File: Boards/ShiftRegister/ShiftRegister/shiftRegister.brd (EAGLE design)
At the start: 100 x 83.8 mm, 18 parts, among them IC1 ARDUINO_PRO_MICRO

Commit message: board
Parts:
- moved R7 49.5 mm to (81.3, 76.2)
- moved R8 48.5 mm to (81.3, 72.4)
- moved R5 48.3 mm to (81.3, 63.5)
- moved R6 48.1 mm to (81.3, 68.6)
- moved R4 47.4 mm to (81.3, 58.4)
- moved R2 46.6 mm to (81.3, 50.8)
- moved R3 46.2 mm to (81.3, 54.6)
- moved R1 45.1 mm to (81.3, 45.7)
- moved IC1 38.6 mm to (16.5, 5.08)
- moved U$1 26.1 mm to (34.3, 57.1), turned to 179.1 degrees
- moved LED7 12.8 mm to (91.4, 68.6)
- moved LED1 8.98 mm to (91.4, 45.7)
- moved LED3 8.98 mm to (91.4, 50.8)
- moved LED4 7.73 mm to (91.4, 54.6)
- moved LED5 6.48 mm to (91.4, 58.4)
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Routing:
- net VCC: track 0.00 -> 25.5 mm, vias 0 -> 1
- added copper zone on layer 16, net GND

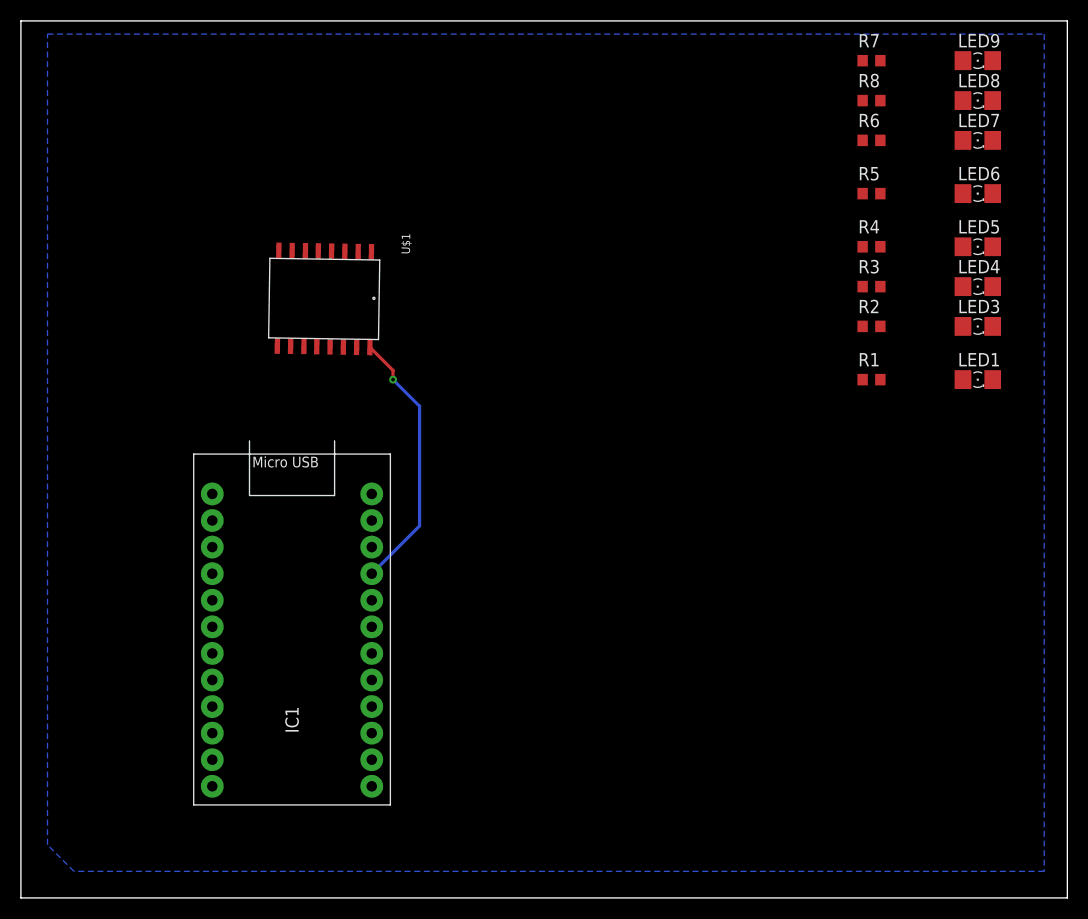
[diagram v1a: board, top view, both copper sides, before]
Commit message: finished board routing ish
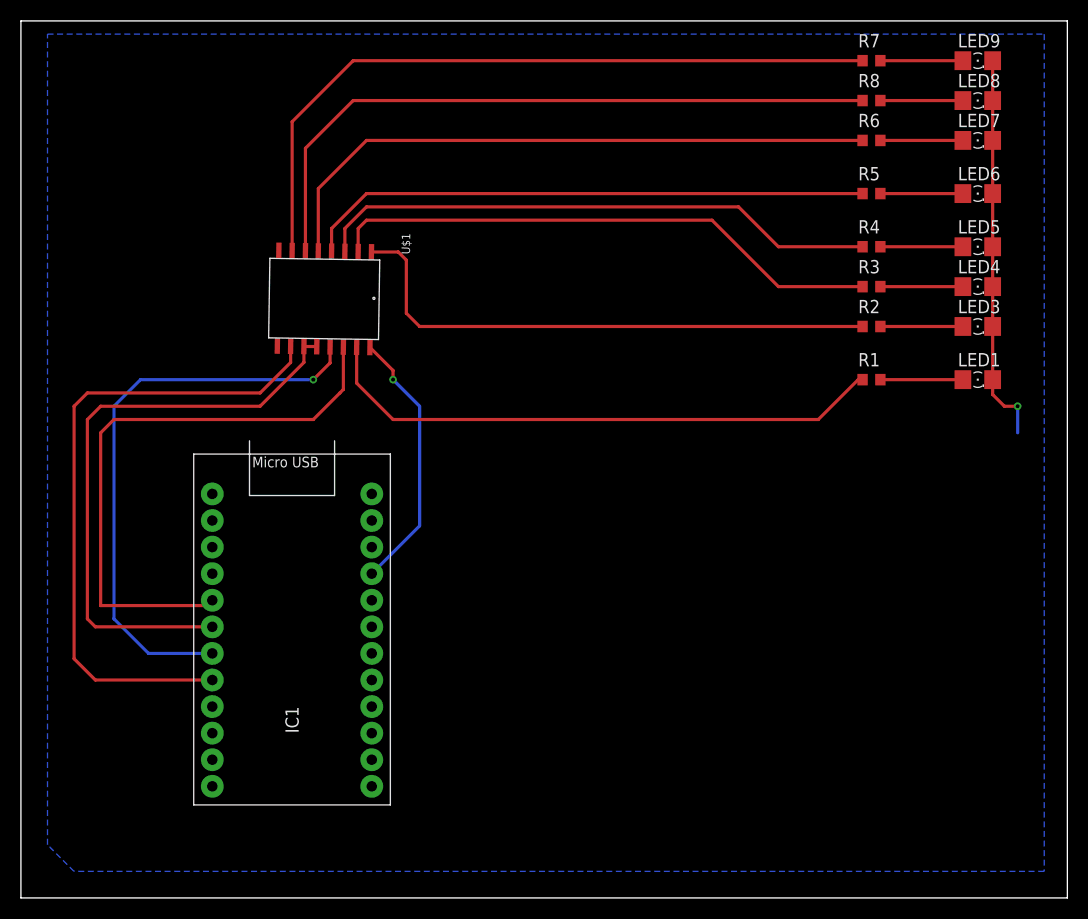
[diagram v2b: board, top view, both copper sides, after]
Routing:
- net QH: track 0.00 -> 69.3 mm
- net QG: track 0.00 -> 64.9 mm
- net SRCLR: track 0.00 -> 62.2 mm
- net QF: track 0.00 -> 59.9 mm
- net CLK: track 0.00 -> 57.0 mm
- net SER: track 0.00 -> 56.4 mm
- net OE: track 0.00 -> 55.0 mm, vias 0 -> 1
- net QA: track 0.00 -> 54.8 mm
- net QE: track 0.00 -> 54.3 mm
- net QD: track 0.00 -> 54.1 mm
- net QC: track 0.00 -> 53.4 mm
- net QB: track 0.00 -> 52.9 mm
- net GND: track 0.00 -> 37.3 mm, vias 0 -> 1
- net N$8: track 0.00 -> 7.89 mm
- net N$7: track 0.00 -> 7.89 mm
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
